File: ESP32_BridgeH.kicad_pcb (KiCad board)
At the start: 2 copper layers, 73.7 x 43.9 mm, 17 parts, among them J1 MT1, J2 MT2, J3 boot, J4 Serial, SW1 reset, U1 TB6612FNG, U2 ESP32-WROOM, U3 MPU6050, U4 LM7833_TO220

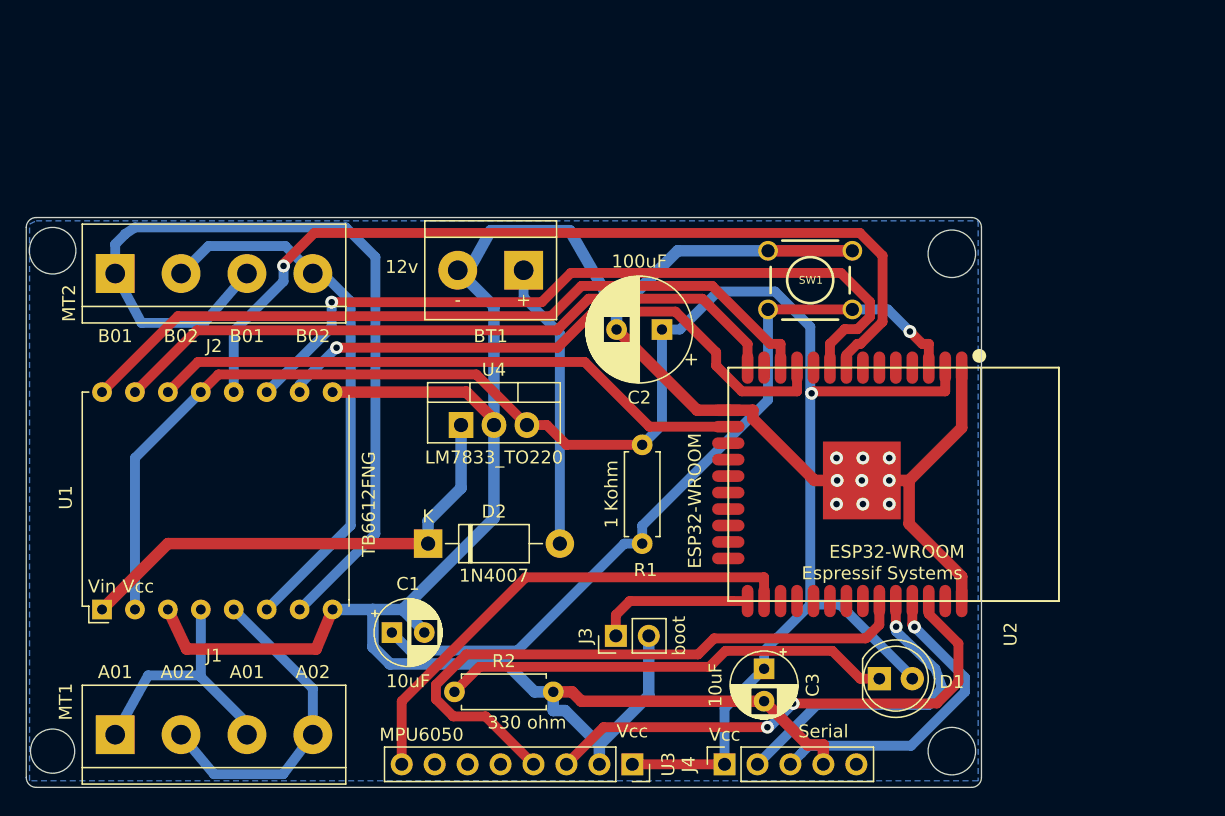
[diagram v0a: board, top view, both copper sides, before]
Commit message: Net update and organizae components
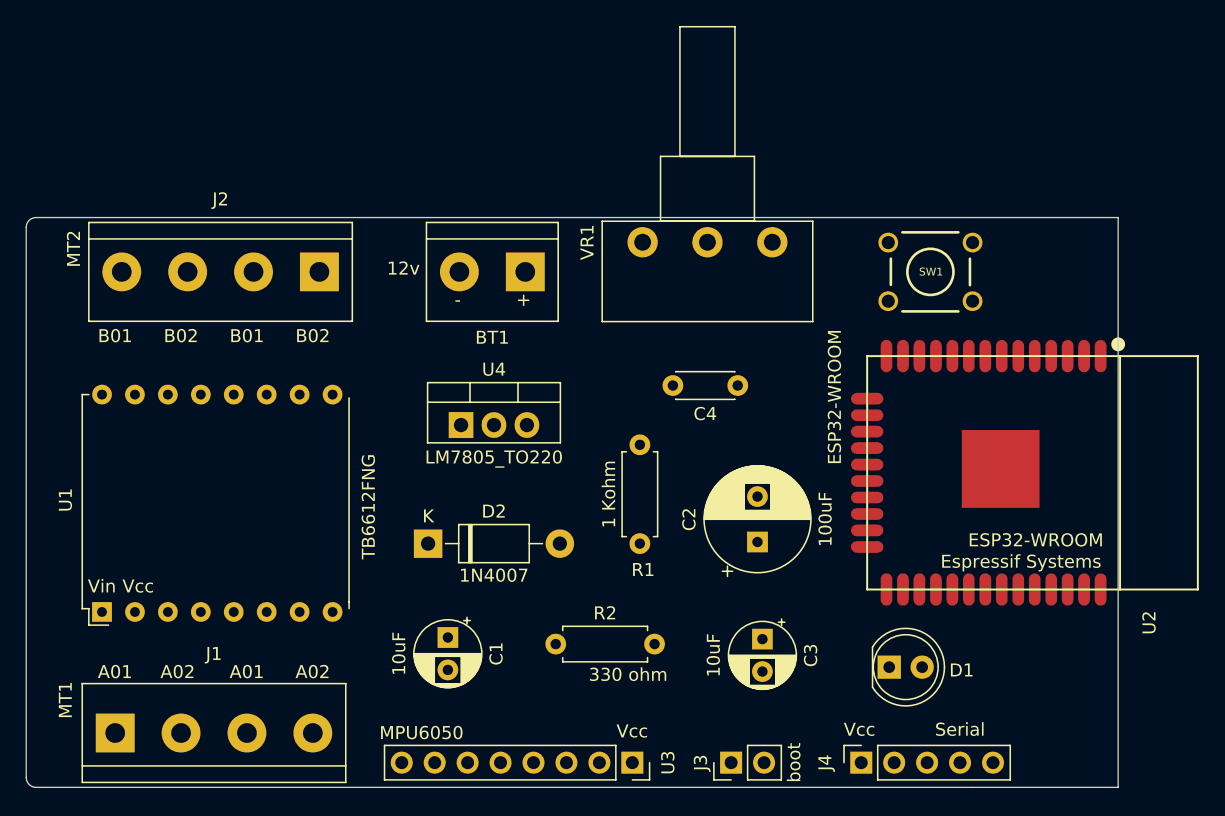
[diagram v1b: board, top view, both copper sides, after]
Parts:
- added C4: 0.1uF, Capacitor_THT:C_Disc_D4.3mm_W1.9mm_P5.00mm, F.Cu at (177.3, 106.7)
- added VR1: POT, Potentiometer_THT:Potentiometer_Piher_T-16H_Single_Horizontal, F.Cu at (180.0, 95.6)
- U4: value LM7833_TO220 -> LM7805_TO220
- moved C2 18.0 mm to (178.8, 118.7), turned to 90 degrees
- moved J2 15.7 mm to (145.0, 97.9), turned to 180 degrees
- moved J3 13.2 mm to (176.8, 135.8)
- moved U2 10.7 mm to (200.0, 113.4)
- moved J4 10.5 mm to (186.8, 135.8)
- moved SW1 9.29 mm to (192.2, 97.9)
- moved R2 8.64 mm to (163.3, 126.6)
- moved C1 4.33 mm to (154.9, 126.1), turned to 270 degrees
- moved C3 2.29 mm to (179.2, 126.2)
- moved D1 1.17 mm to (189.0, 128.4)
- moved U1 0.19 mm to (133.6, 116.5)
- moved R1 0.18 mm to (169.7, 111.3)
- moved BT1 0.18 mm to (160.9, 97.9)
- moved J1 0.13 mm to (129.3, 133.5)
- moved U3 0.13 mm to (169.2, 135.8)
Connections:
- net Net-(U2-Pad13) renamed /ADC
- BT1 pad 1: Net-(BT1-Pad1) -> /Vin
- D2 pad 2: Net-(BT1-Pad1) -> GND
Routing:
- net GND: track 216.4 -> 0.00 mm, vias 9 -> 0
- net /Vcc: track 145.2 -> 0.00 mm, vias 1 -> 0
- net /Bin1: track 69.3 -> 0.00 mm, vias 1 -> 0
- net /B01: track 67.6 -> 0.00 mm
- net /reset: track 60.7 -> 0.00 mm, vias 1 -> 0
- net /PWA: track 59.4 -> 0.00 mm
- net /Bin2: track 59.3 -> 0.00 mm, vias 1 -> 0
- net /Ain1: track 53.5 -> 0.00 mm
- net /SDA: track 48.7 -> 0.00 mm
- net /PWB: track 46.2 -> 0.00 mm, vias 1 -> 0
- net /Ain2: track 46.2 -> 0.00 mm
- net /B02: track 42.2 -> 0.00 mm
- net /SCL: track 40.0 -> 0.00 mm, vias 2 -> 0
- net /INT: track 38.6 -> 0.00 mm
- net /Vin: track 37.4 -> 0.00 mm
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- removed copper zone on B.Cu, net GND
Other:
- board size 73.7 x 43.9 mm -> 84.2 x 43.9 mm

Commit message: Routing
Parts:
- removed VR1: POT, Potentiometer_THT:Potentiometer_Piher_T-16H_Single_Horizontal
- added RV1: R_POT, Potentiometer_THT:Potentiometer_Piher_T-16H_Single_Horizontal, F.Cu at (180.7, 95.6)
- U4: value LM7805_TO220 -> LM7833_TO220
- moved C4 3.99 mm to (173.4, 106.0), turned to 0 degrees
- moved C2 3.49 mm to (179.5, 115.3), turned to 270 degrees
- moved C3 1.27 mm to (178.0, 126.0)
- moved J1 0.77 mm to (130.0, 133.3)
- moved J2 0.77 mm to (145.8, 97.8)
- moved U1 0.77 mm to (134.4, 116.4)
- moved BT1 0.38 mm to (160.5, 97.9)
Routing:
- net GND: track 0.00 -> 250.4 mm, vias 0 -> 1
- net /Vcc: track 0.00 -> 188.3 mm, vias 0 -> 1
- net /Bin2: track 0.00 -> 77.1 mm, vias 0 -> 1
- net /Bin1: track 0.00 -> 73.8 mm
- net /Ain1: track 0.00 -> 73.1 mm
- net /PWA: track 0.00 -> 66.4 mm
- net /reset: track 0.00 -> 64.6 mm, vias 0 -> 1
- net /B01: track 0.00 -> 55.9 mm
- net /Ain2: track 0.00 -> 55.8 mm
- net /PWB: track 0.00 -> 55.1 mm, vias 0 -> 2
- net /INT: track 0.00 -> 53.6 mm, vias 0 -> 1
- net /B02: track 0.00 -> 52.1 mm
- net /Vin: track 0.00 -> 50.4 mm
- net /SDA: track 0.00 -> 48.8 mm, vias 0 -> 3
- net /SCL: track 0.00 -> 48.6 mm, vias 0 -> 3
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- added copper zone on B.Cu, net GND
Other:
- outline, holes or cut-outs redrawn

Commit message: Battery reader and boot correction
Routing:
- net /B02: track 52.1 -> 56.5 mm
- net /B01: track 55.9 -> 56.9 mm
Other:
- board text added: "GND"
- board text added: "Rx"
- board text added: "SCL"
- board text added: "SDA"
- board text added: "Tx"

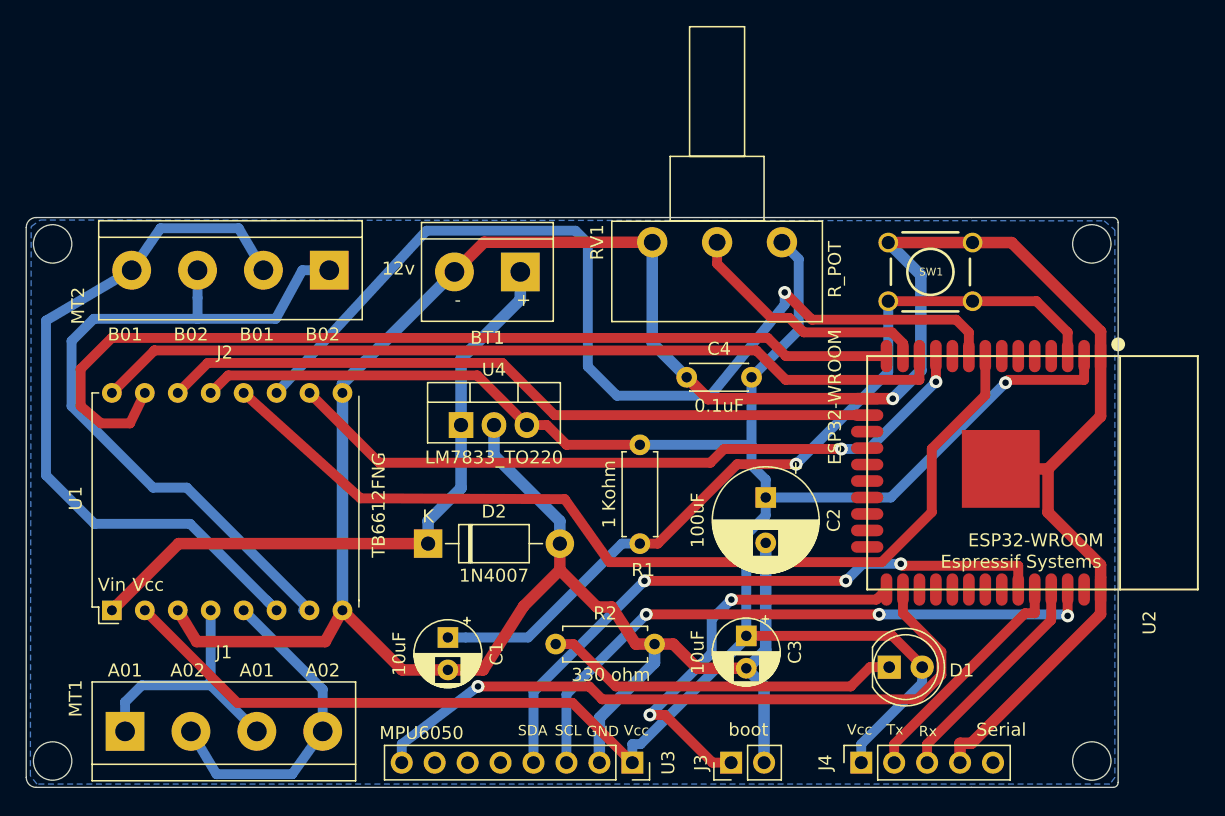
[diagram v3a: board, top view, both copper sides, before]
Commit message: new footprints without routing
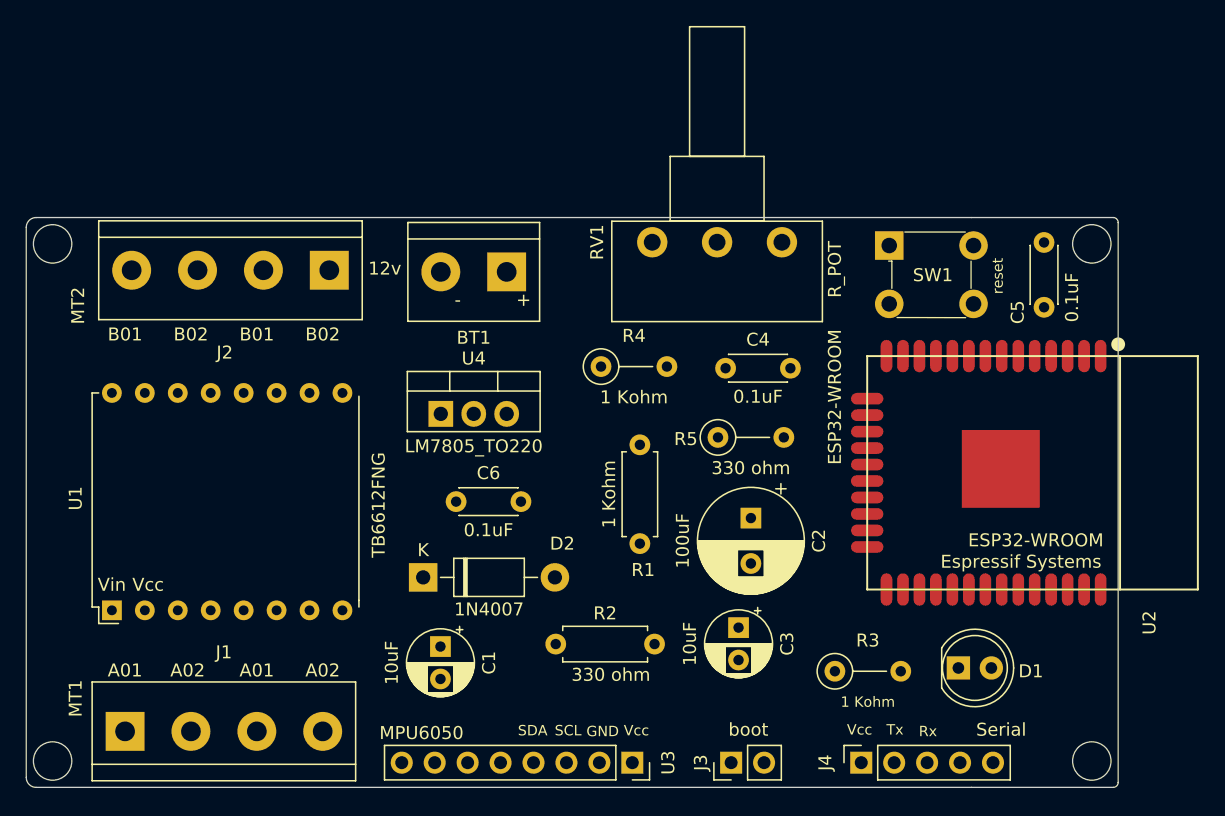
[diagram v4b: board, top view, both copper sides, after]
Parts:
- added C5: 0.1uF, Capacitor_THT:C_Disc_D4.3mm_W1.9mm_P5.00mm, F.Cu at (200.9, 100.6)
- added C6: 0.1uF, Capacitor_THT:C_Disc_D4.3mm_W1.9mm_P5.00mm, F.Cu at (155.6, 115.6)
- added R3: 1 Kohm, Resistor_THT:R_Axial_DIN0207_L6.3mm_D2.5mm_P5.08mm_Vertical, F.Cu at (184.8, 128.7)
- added R4: 1 Kohm, Resistor_THT:R_Axial_DIN0207_L6.3mm_D2.5mm_P5.08mm_Vertical, F.Cu at (166.8, 105.2)
- added R5: 330 ohm, Resistor_THT:R_Axial_DIN0207_L6.3mm_D2.5mm_P5.08mm_Vertical, F.Cu at (175.8, 110.7)
- SW1: footprint freetronics_footprints:SW_PUSHBUTTON_PTH -> digikey-footprints:Switch_Tactile_THT_6x6mm
- U4: value LM7833_TO220 -> LM7805_TO220
- moved D1 5.33 mm to (194.3, 128.5)
- moved SW1 3.77 mm to (189.0, 95.9), turned to 0 degrees
- moved C4 3.08 mm to (176.4, 105.3)
- moved D2 2.63 mm to (153.0, 121.5)
- moved C2 1.96 mm to (178.3, 116.9)
- moved U4 1.78 mm to (154.4, 108.9)
- moved BT1 1.05 mm to (159.5, 97.9)
- moved C1 0.90 mm to (154.4, 126.8)
- moved C3 0.87 mm to (177.4, 125.3)
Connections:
- U2 pad 6: Net-(U2-Pad6) -> /Battery
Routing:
- net GND: track 250.7 -> 0.00 mm, vias 1 -> 0
- net /Vcc: track 188.3 -> 0.00 mm, vias 1 -> 0
- net /Bin2: track 77.1 -> 0.00 mm, vias 1 -> 0
- net /Bin1: track 74.0 -> 0.00 mm
- net /Ain1: track 73.5 -> 0.00 mm
- net /PWA: track 66.4 -> 0.00 mm
- net /reset: track 64.6 -> 0.00 mm, vias 1 -> 0
- net /B01: track 56.9 -> 0.00 mm
- net /B02: track 56.5 -> 0.00 mm
- net /Ain2: track 55.8 -> 0.00 mm
- net /PWB: track 55.1 -> 0.00 mm, vias 2 -> 0
- net /INT: track 53.6 -> 0.00 mm, vias 1 -> 0
- net /Vin: track 50.4 -> 0.00 mm
- net /SDA: track 48.8 -> 0.00 mm, vias 3 -> 0
- net /SCL: track 48.6 -> 0.00 mm, vias 3 -> 0
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- removed copper zone on B.Cu, net GND

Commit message: Routin v2.0 and kicadlogo
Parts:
- added REF**: KiCad-Logo2_6mm_SilkScreen, Symbol:KiCad-Logo2_6mm_SilkScreen, F.Cu at (138.1, 114.2)
- U4: value LM7805_TO220 -> LM7833_TO220
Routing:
- net GND: track 0.00 -> 277.6 mm
- net /Vcc: track 0.00 -> 195.9 mm
- net /reset: track 0.00 -> 91.8 mm, vias 0 -> 2
- net /PWA: track 0.00 -> 69.5 mm, vias 0 -> 2
- net /Ain1: track 0.00 -> 69.4 mm
- net /Bin1: track 0.00 -> 67.7 mm, vias 0 -> 2
- net /Battery: track 0.00 -> 64.3 mm, vias 0 -> 3
- net /Bin2: track 0.00 -> 60.9 mm, vias 0 -> 3
- net /Vin: track 0.00 -> 59.6 mm
- net /Ain2: track 0.00 -> 57.1 mm, vias 0 -> 1
- net /PWB: track 0.00 -> 54.1 mm, vias 0 -> 3
- net /B01: track 0.00 -> 53.9 mm
- net /B02: track 0.00 -> 50.7 mm
- net /SCL: track 0.00 -> 50.6 mm, vias 0 -> 1
- net /INT: track 0.00 -> 50.0 mm
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- added copper zone on B.Cu, net GND

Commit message: JGB v2
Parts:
- U4: value LM7833_TO220 -> LM7805_TO220
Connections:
- C4 pad 2: /Vcc -> /POT
- RV1 pad 2: /ADC -> /POT
- U2 pad 13: /ADC -> /POT
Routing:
- net GND: track 277.6 -> 174.5 mm, vias 0 -> 7
- net /Vin: track 59.6 -> 116.8 mm
- net /POT: track 0.00 -> 26.9 mm, vias 0 -> 1
- net /ADC: track 19.3 -> 0.00 mm
- net /Vcc: track 195.9 -> 206.7 mm, vias 0 -> 2
- net Net-(U2-Pad37): track 0.00 -> 7.56 mm, vias 0 -> 1
- net /PWB: track 54.1 -> 60.9 mm
- net /B02: track 50.7 -> 56.2 mm
- net /B01: track 53.9 -> 59.3 mm
- net Net-(U2-Pad23): track 0.00 -> 3.45 mm, vias 0 -> 1
- net /A02: track 25.6 -> 28.8 mm
- net /Ain1: track 69.4 -> 72.0 mm
- net /reset: track 91.8 -> 94.3 mm
- net Net-(D1-Pad1): track 34.0 -> 35.9 mm
- net /PWA: track 69.5 -> 71.0 mm
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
